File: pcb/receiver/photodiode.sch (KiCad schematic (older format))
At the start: 118 parts, among them Q201 BFR31,215, Q202 MMBT2222A-7-F, Q203 MMBT2222A-7-F, Q204 MMBT2222A-7-F, Q205 MMBT2222A-7-F, Q206 MMBT2222A-7-F, Q207 TF414T5G, U201 ADR550ARTZ-REEL7, U202 TL974IPWR, U203 MAX4477AUA+, U204 OPA2141AIDR, U205 NLAS4599DFT2G

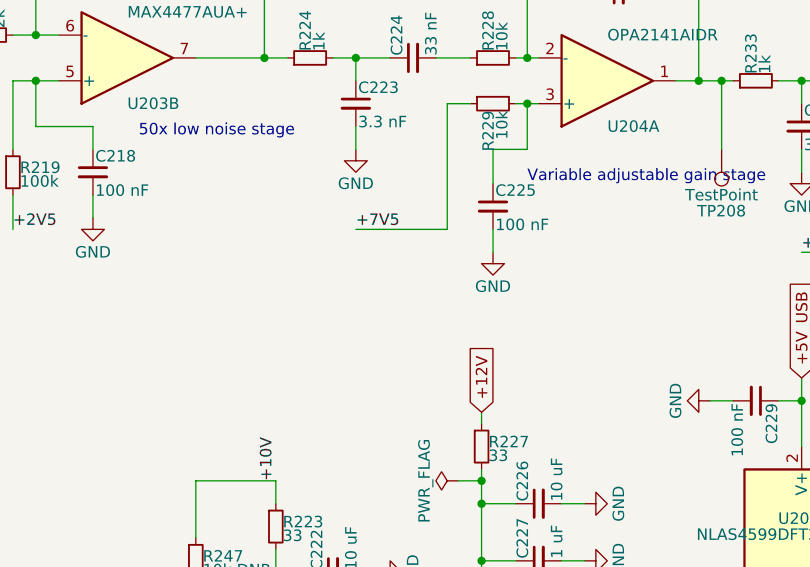
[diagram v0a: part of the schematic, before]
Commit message: Note missing components
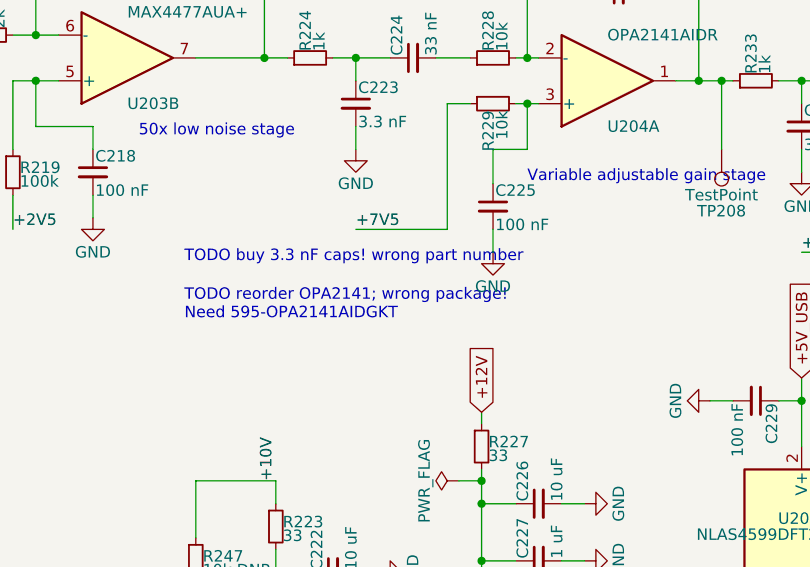
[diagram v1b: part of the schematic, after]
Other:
- note added: "TODO buy 3.3 nF caps! wrong part number"
- note added: "TODO reorder OPA2141; wrong package!\nNeed 595-OPA2141AIDGKT\n"
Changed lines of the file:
@@
 Wire Wire Line
 	1100 1800 1650 1800
+Text Notes 6200 4200 0    50   ~ 0
+TODO buy 3.3 nF caps! wrong part number
+Text Notes 6200 4450 0    50   ~ 0
+TODO reorder OPA2141; wrong package!\nNeed 595-OPA2141AIDGKT\n
 $EndSCHEMATC

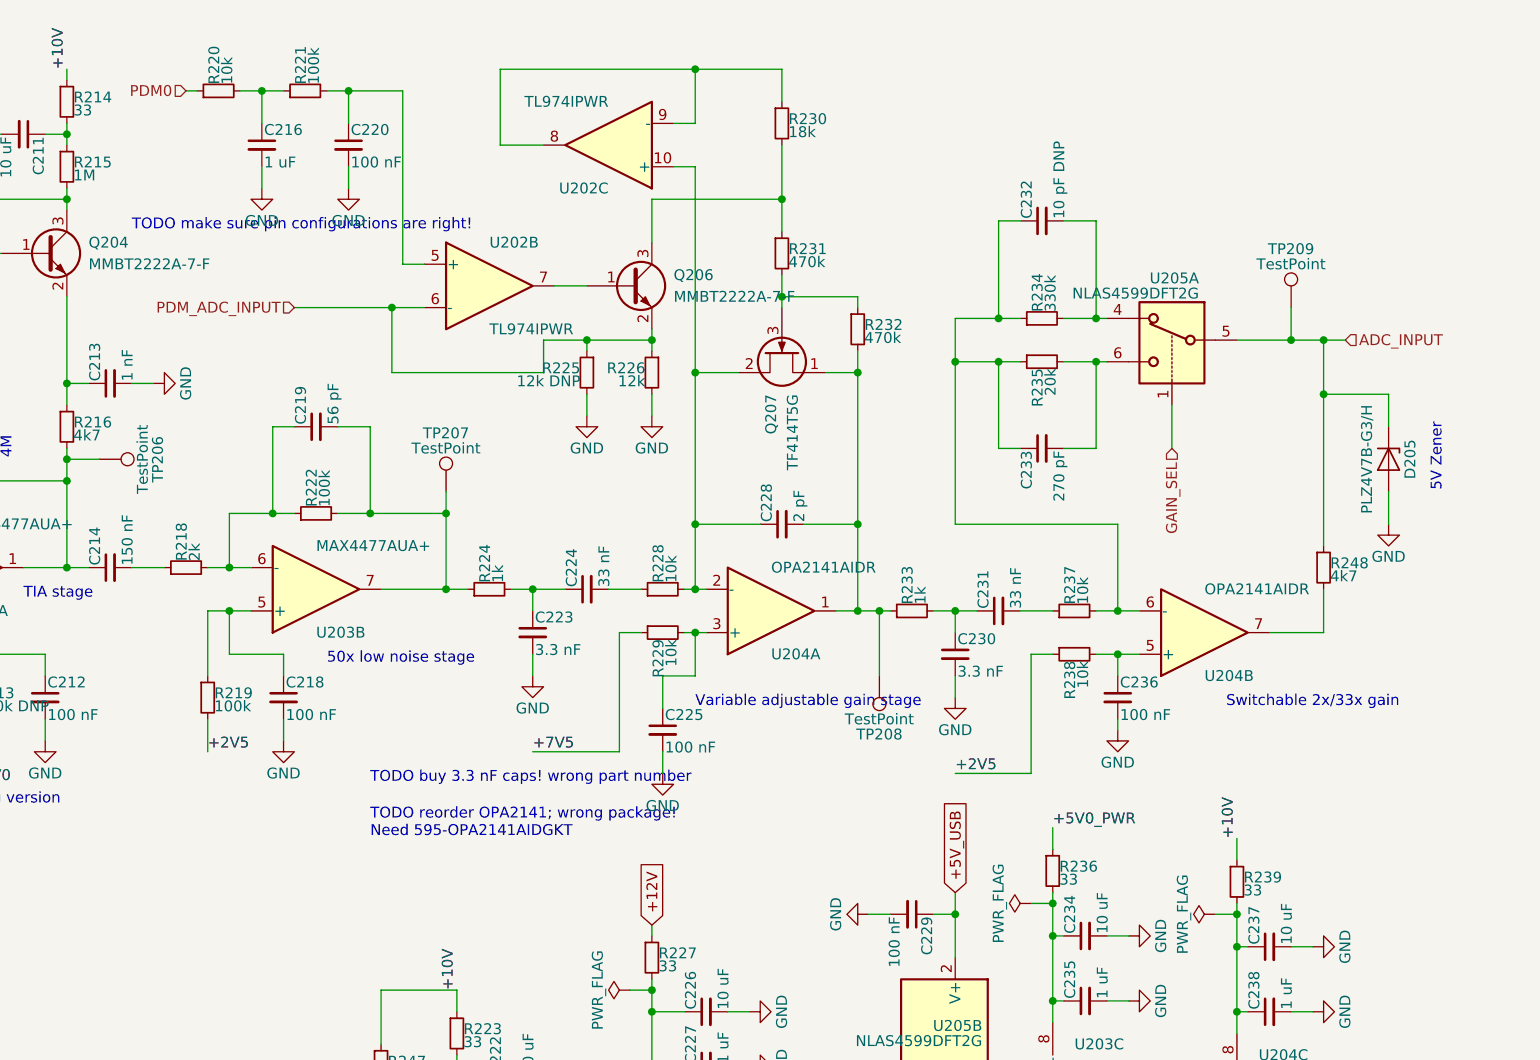
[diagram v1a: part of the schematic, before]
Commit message: Add in TODOs for a lot of small mistakes
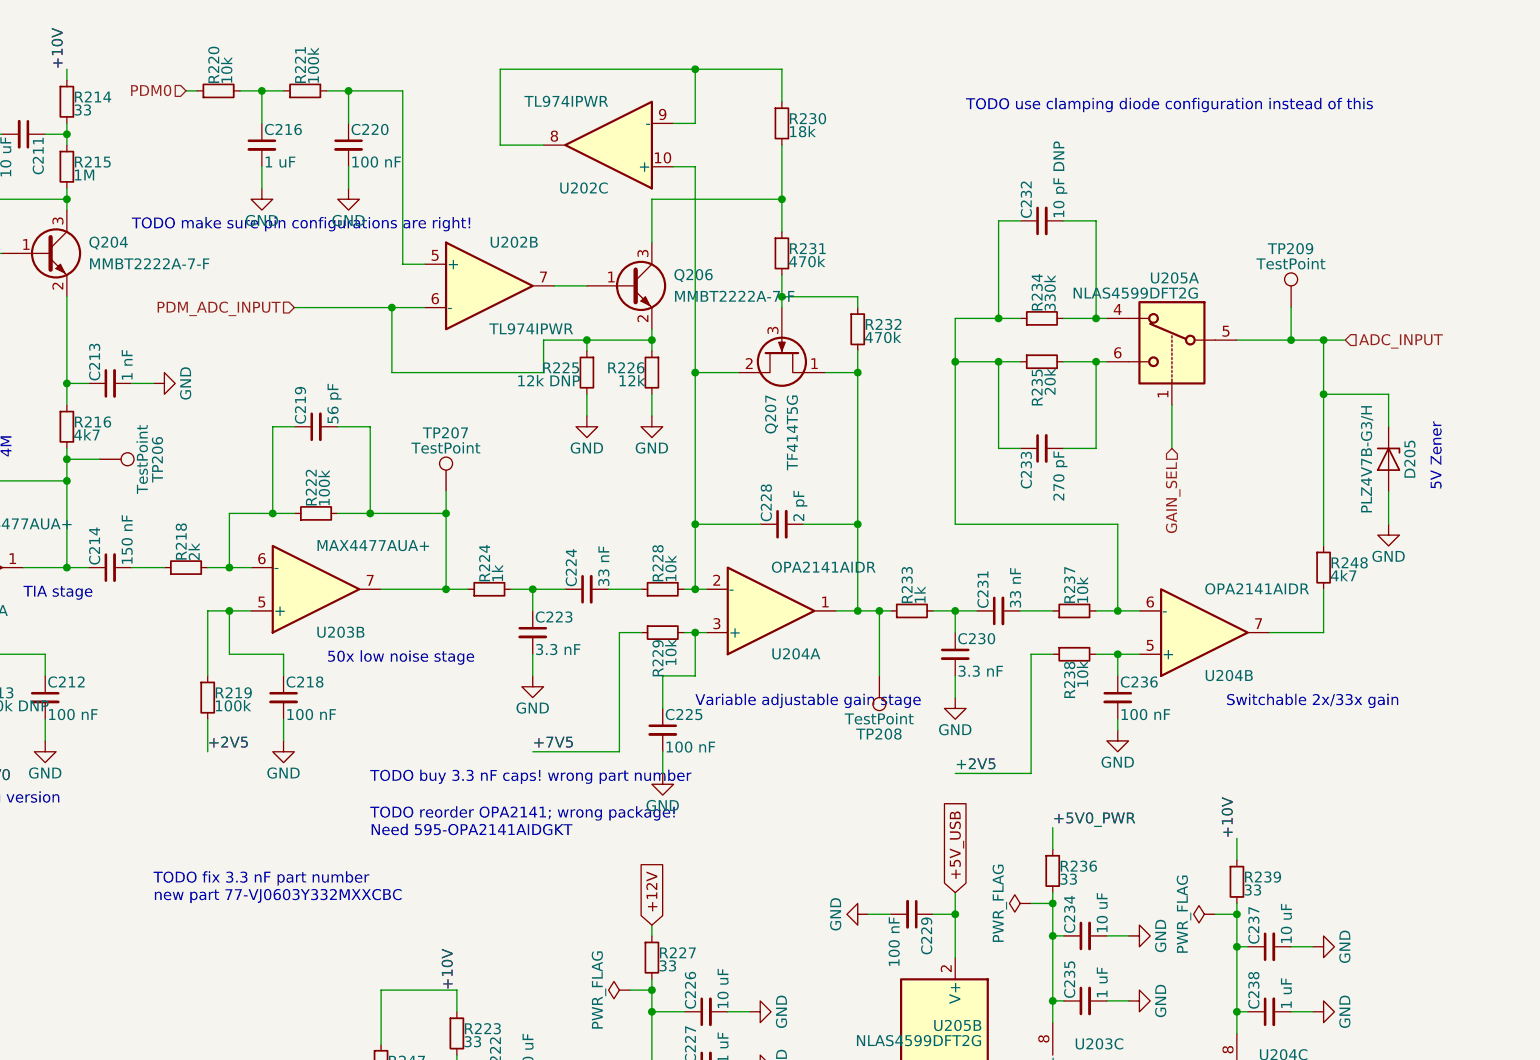
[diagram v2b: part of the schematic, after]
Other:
- note added: "TODO fix 3.3 nF part number\nnew part 77-VJ0603Y332MXXCBC\n"
- note added: "TODO use clamping diode configuration instead of this"
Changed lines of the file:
@@
 Text Notes 6200 4450 0    50   ~ 0
 TODO reorder OPA2141; wrong package!\nNeed 595-OPA2141AIDGKT\n
+Text Notes 5200 4750 0    50   ~ 0
+TODO fix 3.3 nF part number\nnew part 77-VJ0603Y332MXXCBC\n
+Text Notes 8950 1100 0    50   ~ 0
+TODO use clamping diode configuration instead of this
 $EndSCHEMATC

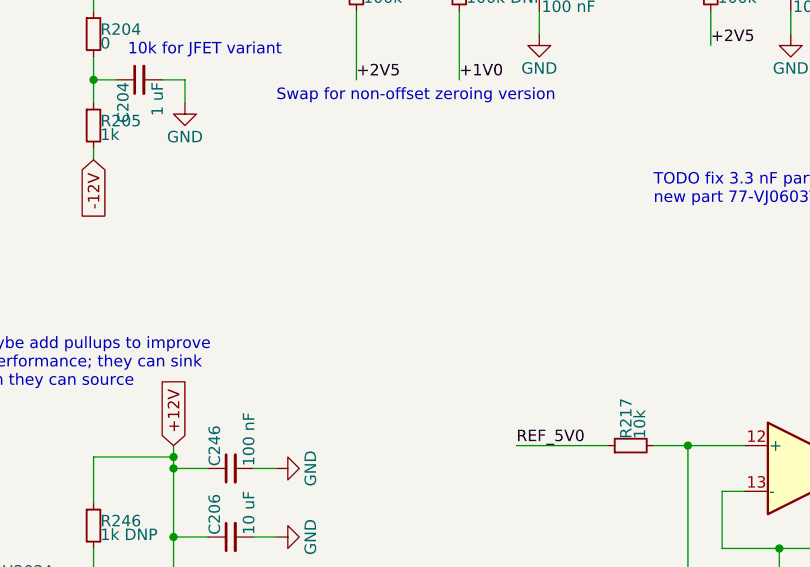
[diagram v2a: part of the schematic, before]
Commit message: Add note for swapping out power supply op amp
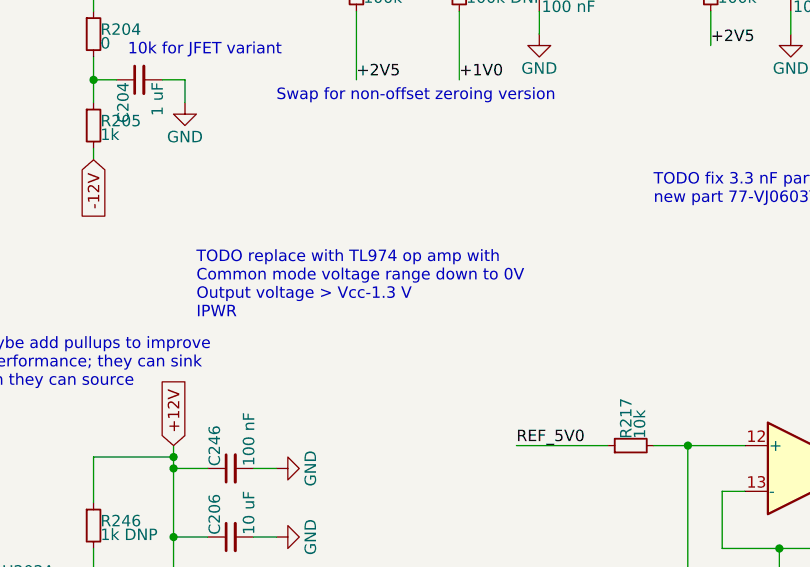
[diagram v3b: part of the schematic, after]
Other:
- note added: "TODO replace with TL974 op amp with \nCommon mode voltage range down to 0V\nOutput voltage > Vcc-1.3 V\nIPWR"
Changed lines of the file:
@@
 Text Notes 8950 1100 0    50   ~ 0
 TODO use clamping diode configuration instead of this
+Text Notes 3200 5250 0    50   ~ 0
+TODO replace with TL974 op amp with \nCommon mode voltage range down to 0V\nOutput voltage > Vcc-1.3 V\nIPWR
 $EndSCHEMATC
